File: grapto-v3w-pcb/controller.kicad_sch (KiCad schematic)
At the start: 31 parts, among them J5 Conn_01x06_Female, J6 USB_C_Receptacle_USB2.0, J7 USB_C_Receptacle_USB2.0, J8 Conn_01x06_Male, U11 USBLC6-4SC6, U12 ACN52840, U13 TPS2110, U14 LM3676SD-3.3

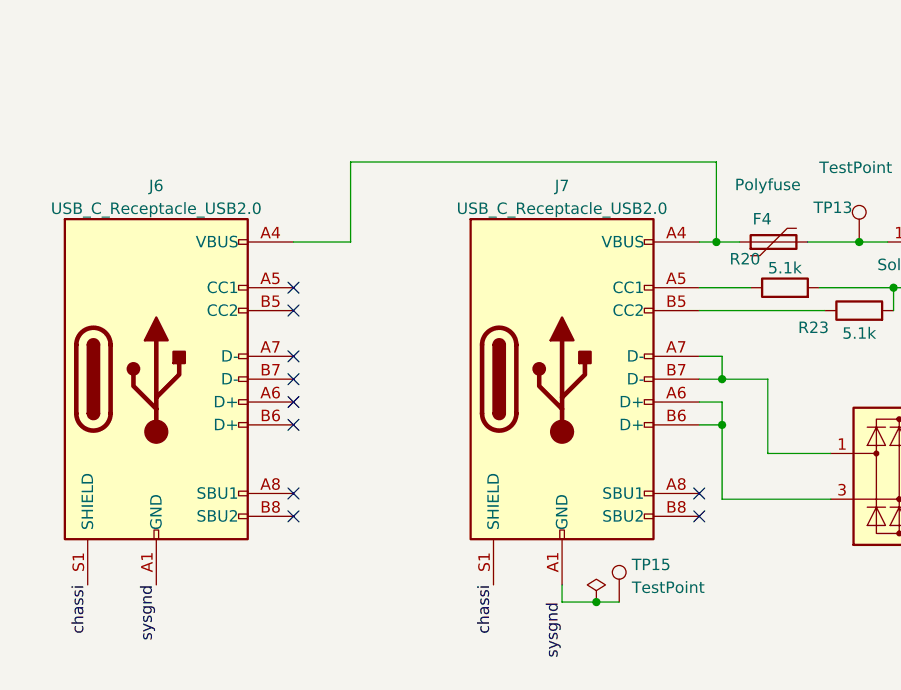
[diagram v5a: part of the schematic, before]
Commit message: Began case rework.
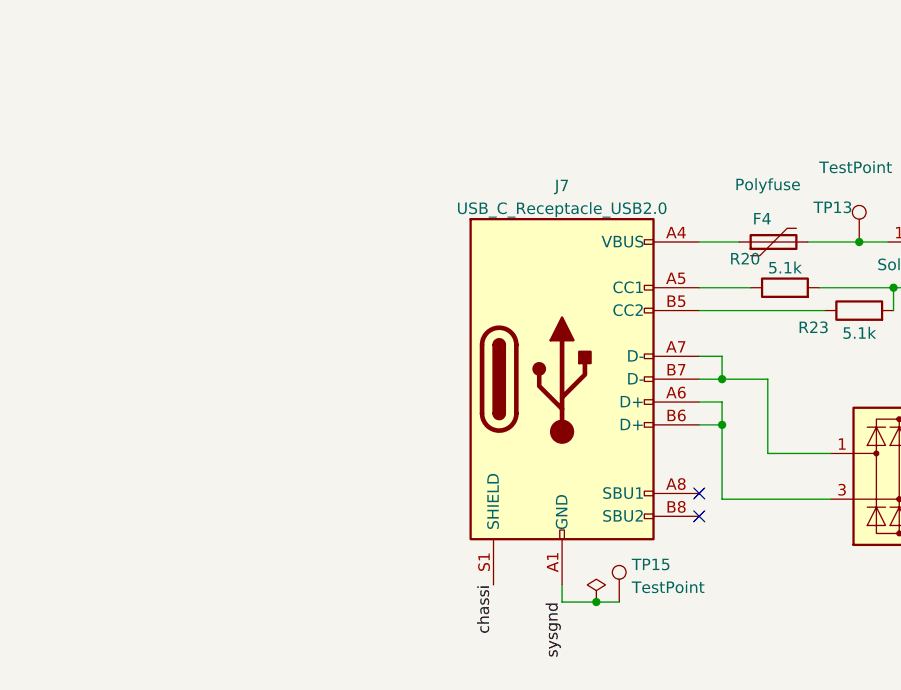
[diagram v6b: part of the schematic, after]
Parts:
- removed J6: USB_C_Receptacle_USB2.0, grapto-v3w:USB_C_Receptacle_molex_2169900001, symbol Connector:USB_C_Receptacle_USB2.0
- J7: footprint (none) -> grapto-v3w:USB_C_Receptacle_molex_2169900001
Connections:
- no-connect marks 23 -> 15
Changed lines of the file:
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@@
   (junction (at 100.965 157.48) (diameter 0) (color 0 0 0 0)
   )
-  (junction (at 100.33 137.16) (diameter 0) (color 0 0 0 0)
-  )
   (junction (at 149.86 59.69) (diameter 0) (color 0 0 0 0)
   )
-  (no_connect (at 53.34 149.86))
   (no_connect (at 38.1 45.72))
-  (no_connect (at 53.34 144.78))
   (no_connect (at 38.1 40.64))
-  (no_connect (at 53.34 154.94))
-  (no_connect (at 53.34 152.4))
-  (no_connect (at 53.34 167.64))
-  (no_connect (at 53.34 165.1))
   (no_connect (at 178.435 130.81))
   (no_connect (at 178.435 125.73))
@@
   (no_connect (at 201.295 143.51))
   (no_connect (at 203.835 143.51))
-  (no_connect (at 53.34 157.48))
   (no_connect (at 38.1 43.18))
   (no_connect (at 98.425 165.1))
   (no_connect (at 38.1 48.26))
-  (no_connect (at 53.34 142.24))
   (no_connect (at 98.425 167.64))
   (no_connect (at 124.46 36.195))
-  (wire (pts (xy 100.33 128.27) (xy 100.33 137.16))
-    (stroke (width 0) (type default) (color 0 0 0 0))
-  )
   (wire (pts (xy 98.425 154.94) (xy 100.965 154.94))
     (stroke (width 0) (type default) (color 0 0 0 0))
@@
     (stroke (width 0) (type default) (color 0 0 0 0))
   )
-  (wire (pts (xy 100.33 137.16) (xy 102.87 137.16))
-    (stroke (width 0) (type default) (color 0 0 0 0))
-  )
   (wire (pts (xy 243.205 54.61) (xy 243.205 58.42))
     (stroke (width 0) (type default) (color 0 0 0 0))
@@
     (stroke (width 0) (type default) (color 0 0 0 0))
   )
-  (wire (pts (xy 59.69 137.16) (xy 59.69 128.27))
-    (stroke (width 0) (type default) (color 0 0 0 0))
-  )
   (wire (pts (xy 45.72 55.245) (xy 45.72 49.53))
     (stroke (width 0) (type default) (color 0 0 0 0))
@@
     (stroke (width 0) (type default) (color 0 0 0 0))
   )
-  (wire (pts (xy 59.69 128.27) (xy 100.33 128.27))
-    (stroke (width 0) (type default) (color 0 0 0 0))
-  )
   (wire (pts (xy 165.735 43.815) (xy 165.735 45.085))
     (stroke (width 0) (type default) (color 0 0 0 0))
@@
     (stroke (width 0) (type default) (color 0 0 0 0))
   )
-  (wire (pts (xy 53.34 137.16) (xy 59.69 137.16))
-    (stroke (width 0) (type default) (color 0 0 0 0))
-  )
   (wire (pts (xy 114.935 59.69) (xy 114.935 59.055))
     (stroke (width 0) (type default) (color 0 0 0 0))
@@
     (stroke (width 0) (type default) (color 0 0 0 0))
   )
-  (wire (pts (xy 98.425 137.16) (xy 100.33 137.16))
+  (wire (pts (xy 98.425 137.16) (xy 102.87 137.16))
     (stroke (width 0) (type default) (color 0 0 0 0))
   )
@@
     (effects (font (size 1.27 1.27)) (justify right bottom))
   )
-  (label "sysgnd" (at 38.1 175.26 270)
-    (effects (font (size 1.27 1.27)) (justify right bottom))
-  )
   (label "col0" (at 178.435 107.95 180)
     (effects (font (size 1.27 1.27)) (justify right bottom))
@@
     (effects (font (size 1.27 1.27)) (justify right bottom))
   )
-  (label "chassi" (at 30.48 175.26 270)
-    (effects (font (size 1.27 1.27)) (justify right bottom))
-  )
   (label "3.3v" (at 178.435 133.35 180)
     (effects (font (size 1.27 1.27)) (justify right bottom))
@@
   (label "p+" (at 165.735 52.07 0)
     (effects (font (size 1.27 1.27)) (justify left bottom))
-  )
-  (symbol (lib_id "Connector:USB_C_Receptacle_USB2.0") (at 38.1 152.4 0) (unit 1)
-    (in_bom yes) (on_board yes) (fields_autoplaced)
-    (property "Reference" "J6" (id 0) (at 38.1 130.9202 0))
-    (property "Value" "USB_C_Receptacle_USB2.0" (id 1) (at 38.1 133.4571 0))
-    (property "Footprint" "grapto-v3w:USB_C_Receptacle_molex_2169900001" (id 2) (at 41.91 152.4 0)
-      (effects (font (size 1.27 1.27)) hide)
-    )
-    (property "Datasheet" "https://www.usb.org/sites/default/files/documents/usb_type-c.zip" (id 3) (at 41.91 152.4 0)
-      (effects (font (size 1.27 1.27)) hide)
-    )
-    (pin "A1")
-    (pin "A12")
-    (pin "A4")
-    (pin "A5")
-    (pin "A6")
-    (pin "A7")
-    (pin "A8")
-    (pin "A9")
-    (pin "B1")
-    (pin "B12")
-    (pin "B4")
-    (pin "B5")
-    (pin "B6")
-    (pin "B7")
-    (pin "B8")
-    (pin "B9")
-    (pin "S1")
   )
   (symbol (lib_id "Device:R") (at 106.68 50.8 0) (unit 1)
@@
     (property "Reference" "J7" (id 0) (at 83.185 130.9202 0))
     (property "Value" "USB_C_Receptacle_USB2.0" (id 1) (at 83.185 133.4571 0))
-    (property "Footprint" "" (id 2) (at 86.995 152.4 0)
-      (effects (font (size 1.27 1.27)) hide)
-    )
+    (property "Footprint" "grapto-v3w:USB_C_Receptacle_molex_2169900001" (id 2) (at 86.995 152.4 0)
+      (effects (font (size 1.27 1.27)) hide)
+    )

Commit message: flipping usbs
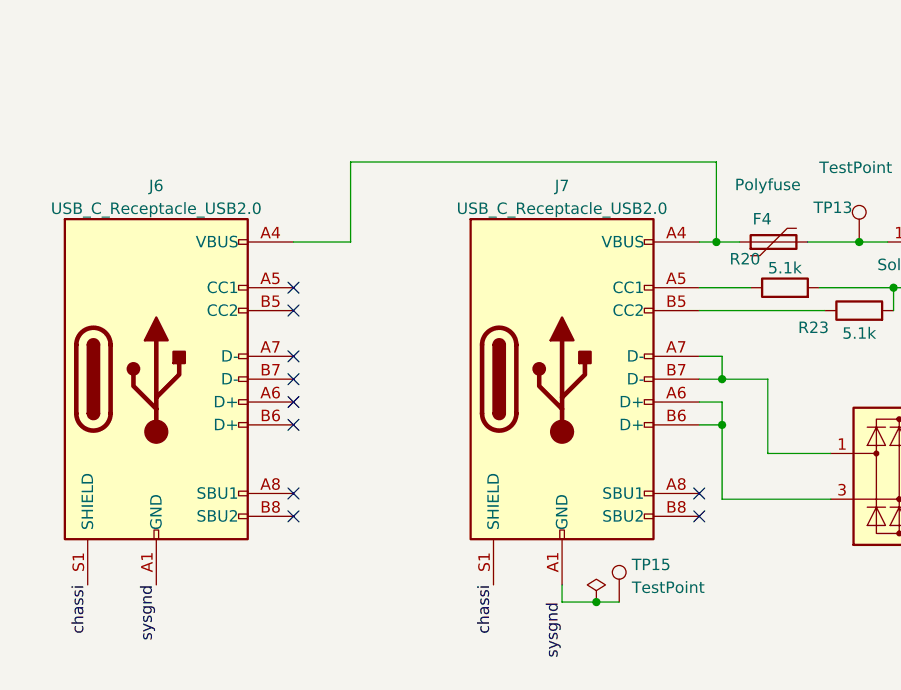
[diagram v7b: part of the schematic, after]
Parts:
- added J6: USB_C_Receptacle_USB2.0, grapto-v3w:USB_C_Receptacle_molex_2169900001, symbol Connector:USB_C_Receptacle_USB2.0
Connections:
- net chassi: now also J6.S1 (SHIELD)
- net sysgnd: now also J6.A1 (GND), J6.A12 (GND), J6.B1 (GND), J6.B12 (GND)
- net at F4.1, J7.A4 (VBUS), J7.A9 (VBUS)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: now also J6.A4 (VBUS), J6.A9 (VBUS), J6.B4 (VBUS), J6.B9 (VBUS)
- no-connect marks 15 -> 23
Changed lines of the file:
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@@
   (junction (at 100.965 157.48) (diameter 0) (color 0 0 0 0)
   )
+  (junction (at 100.33 137.16) (diameter 0) (color 0 0 0 0)
+  )
   (junction (at 149.86 59.69) (diameter 0) (color 0 0 0 0)
   )
+  (no_connect (at 53.34 149.86))
   (no_connect (at 38.1 45.72))
+  (no_connect (at 53.34 144.78))
   (no_connect (at 38.1 40.64))
+  (no_connect (at 53.34 154.94))
+  (no_connect (at 53.34 152.4))
+  (no_connect (at 53.34 167.64))
+  (no_connect (at 53.34 165.1))
   (no_connect (at 178.435 130.81))
   (no_connect (at 178.435 125.73))
@@
   (no_connect (at 201.295 143.51))
   (no_connect (at 203.835 143.51))
+  (no_connect (at 53.34 157.48))
   (no_connect (at 38.1 43.18))
   (no_connect (at 98.425 165.1))
   (no_connect (at 38.1 48.26))
+  (no_connect (at 53.34 142.24))
   (no_connect (at 98.425 167.64))
   (no_connect (at 124.46 36.195))
+  (wire (pts (xy 100.33 128.27) (xy 100.33 137.16))
+    (stroke (width 0) (type default) (color 0 0 0 0))
+  )
   (wire (pts (xy 98.425 154.94) (xy 100.965 154.94))
     (stroke (width 0) (type default) (color 0 0 0 0))
@@
     (stroke (width 0) (type default) (color 0 0 0 0))
   )
+  (wire (pts (xy 100.33 137.16) (xy 102.87 137.16))
+    (stroke (width 0) (type default) (color 0 0 0 0))
+  )
   (wire (pts (xy 243.205 54.61) (xy 243.205 58.42))
     (stroke (width 0) (type default) (color 0 0 0 0))
@@
     (stroke (width 0) (type default) (color 0 0 0 0))
   )
+  (wire (pts (xy 59.69 137.16) (xy 59.69 128.27))
+    (stroke (width 0) (type default) (color 0 0 0 0))
+  )
   (wire (pts (xy 45.72 55.245) (xy 45.72 49.53))
     (stroke (width 0) (type default) (color 0 0 0 0))
@@
     (stroke (width 0) (type default) (color 0 0 0 0))
   )
+  (wire (pts (xy 59.69 128.27) (xy 100.33 128.27))
+    (stroke (width 0) (type default) (color 0 0 0 0))
+  )
   (wire (pts (xy 165.735 43.815) (xy 165.735 45.085))
     (stroke (width 0) (type default) (color 0 0 0 0))
@@
     (stroke (width 0) (type default) (color 0 0 0 0))
   )
+  (wire (pts (xy 53.34 137.16) (xy 59.69 137.16))
+    (stroke (width 0) (type default) (color 0 0 0 0))
+  )
   (wire (pts (xy 114.935 59.69) (xy 114.935 59.055))
     (stroke (width 0) (type default) (color 0 0 0 0))
@@
     (stroke (width 0) (type default) (color 0 0 0 0))
   )
-  (wire (pts (xy 98.425 137.16) (xy 102.87 137.16))
+  (wire (pts (xy 98.425 137.16) (xy 100.33 137.16))
     (stroke (width 0) (type default) (color 0 0 0 0))
   )
@@
     (effects (font (size 1.27 1.27)) (justify right bottom))
   )
+  (label "sysgnd" (at 38.1 175.26 270)
+    (effects (font (size 1.27 1.27)) (justify right bottom))
+  )
   (label "col0" (at 178.435 107.95 180)
     (effects (font (size 1.27 1.27)) (justify right bottom))
@@
     (effects (font (size 1.27 1.27)) (justify right bottom))
   )
+  (label "chassi" (at 30.48 175.26 270)
+    (effects (font (size 1.27 1.27)) (justify right bottom))
+  )
   (label "3.3v" (at 178.435 133.35 180)
     (effects (font (size 1.27 1.27)) (justify right bottom))
@@
     (effects (font (size 1.27 1.27)) (justify left bottom))
   )
+  (symbol (lib_id "Connector:USB_C_Receptacle_USB2.0") (at 38.1 152.4 0) (unit 1)
+    (in_bom yes) (on_board yes) (fields_autoplaced)
+    (property "Reference" "J6" (id 0) (at 38.1 130.9202 0))
+    (property "Value" "USB_C_Receptacle_USB2.0" (id 1) (at 38.1 133.4571 0))
+    (property "Footprint" "grapto-v3w:USB_C_Receptacle_molex_2169900001" (id 2) (at 41.91 152.4 0)
+      (effects (font (size 1.27 1.27)) hide)
+    )
+    (property "Datasheet" "https://www.usb.org/sites/default/files/documents/usb_type-c.zip" (id 3) (at 41.91 152.4 0)
+      (effects (font (size 1.27 1.27)) hide)
+    )
+    (pin "A1")
+    (pin "A12")
+    (pin "A4")
+    (pin "A5")
+    (pin "A6")
+    (pin "A7")
+    (pin "A8")
+    (pin "A9")
+    (pin "B1")
+    (pin "B12")
+    (pin "B4")
+    (pin "B5")
+    (pin "B6")
+    (pin "B7")
+    (pin "B8")
+    (pin "B9")
+    (pin "S1")
+  )
   (symbol (lib_id "Device:R") (at 106.68 50.8 0) (unit 1)

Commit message: Added snap supports.
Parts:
- added TP19: ~, symbol Connector:TestPoint
- added TP20, TP21: (no value), symbol Connector:TestPoint
- TP13, TP14, TP15, TP16, TP17, TP18: footprint TestPoint:TestPoint_Pad_2.0x2.0mm -> (none)
- U12: footprint grapto-v3w:ACN52840_mirror -> (none)
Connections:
- net low_batt: now also TP19.1
- net scl: now also TP20.1
- net sda: now also TP21.1
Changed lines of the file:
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@@
+    (stroke (width 0) (type default) (color 0 0 0 0))
+  )
+  (wire (pts (xy 72.39 38.1) (xy 83.82 38.1))
     (stroke (width 0) (type default) (color 0 0 0 0))
   )
@@
     (effects (font (size 1.27 1.27)) (justify right bottom))
   )
-  (label "scl" (at 250.825 120.65 180)
+  (label "scl" (at 250.825 118.745 180)
     (effects (font (size 1.27 1.27)) (justify right bottom))
   )
@@
     (effects (font (size 1.27 1.27)) (justify left bottom))
   )
-  (label "sda" (at 258.445 120.65 0)
+  (label "sda" (at 258.445 118.745 0)
     (effects (font (size 1.27 1.27)) (justify left bottom))
   )
@@
       (effects (font (size 1.27 1.27)) (justify left))
     )
-    (property "Footprint" "TestPoint:TestPoint_Pad_2.0x2.0mm" (id 2) (at 255.905 46.99 0)
+    (property "Footprint" "" (id 2) (at 255.905 46.99 0)
       (effects (font (size 1.27 1.27)) hide)
     )
@@
     (pin "2")
   )
+  (symbol (lib_id "Connector:TestPoint") (at 258.445 120.65 270) (unit 1)
+    (in_bom yes) (on_board yes) (fields_autoplaced)
+    (property "Reference" "TP21" (id 0) (at 263.144 119.8153 90)
+      (effects (font (size 1.27 1.27)) (justify left))
+    )
+    (property "Value" "" (id 1) (at 263.144 122.3522 90)
+      (effects (font (size 1.27 1.27)) (justify left))
+    )
+    (property "Footprint" "" (id 2) (at 258.445 125.73 0)
+      (effects (font (size 1.27 1.27)) hide)
+    )
+    (property "Datasheet" "~" (id 3) (at 258.445 125.73 0)
+      (effects (font (size 1.27 1.27)) hide)
+    )
+    (pin "1")
+  )
   (symbol (lib_id "Device:C") (at 243.205 50.8 0) (unit 1)
     (in_bom yes) (on_board yes) (fields_autoplaced)
@@
     (pin "1")
     (pin "2")
+  )
+  (symbol (lib_id "Connector:TestPoint") (at 83.82 38.1 0) (unit 1)
+    (in_bom yes) (on_board yes)
+    (property "Reference" "TP19" (id 0) (at 84.455 31.75 90))
+    (property "Value" "~" (id 1) (at 81.915 34.925 90))
+    (property "Footprint" "" (id 2) (at 88.9 38.1 0)
+      (effects (font (size 1.27 1.27)) hide)
+    )
+    (property "Datasheet" "~" (id 3) (at 88.9 38.1 0)
+      (effects (font (size 1.27 1.27)) hide)
+    )
+    (pin "1")
   )
   (symbol (lib_id "Connector:USB_C_Receptacle_USB2.0") (at 83.185 152.4 0) (unit 1)
@@
     (property "Reference" "U12" (id 0) (at 198.12 99.221 0))
     (property "Value" "ACN52840" (id 1) (at 198.12 101.7579 0))
-    (property "Footprint" "grapto-v3w:ACN52840_mirror" (id 2) (at 207.645 147.32 0)
+    (property "Footprint" "" (id 2) (at 207.645 147.32 0)
       (effects (font (size 1.27 1.27)) hide)
     )
@@
       (effects (font (size 1.27 1.27)) (justify left))
     )
-    (property "Footprint" "TestPoint:TestPoint_Pad_2.0x2.0mm" (id 2) (at 94.615 177.165 0)
+    (property "Footprint" "" (id 2) (at 94.615 177.165 0)
       (effects (font (size 1.27 1.27)) hide)
     )
@@
       (effects (font (size 1.27 1.27)) (justify left))
     )
-    (property "Footprint" "TestPoint:TestPoint_Pad_2.0x2.0mm" (id 2) (at 135.255 137.16 0)
+    (property "Footprint" "" (id 2) (at 135.255 137.16 0)
       (effects (font (size 1.27 1.27)) hide)
     )
@@
       (effects (font (size 1.27 1.27)) (justify left))
     )
-    (property "Footprint" "TestPoint:TestPoint_Pad_2.0x2.0mm" (id 2) (at 121.285 137.16 0)
+    (property "Footprint" "" (id 2) (at 121.285 137.16 0)
       (effects (font (size 1.27 1.27)) hide)
     )
     (property "Datasheet" "~" (id 3) (at 121.285 137.16 0)
+      (effects (font (size 1.27 1.27)) hide)
+    )
+    (pin "1")
+  )
+  (symbol (lib_id "Connector:TestPoint") (at 250.825 120.65 90) (unit 1)
+    (in_bom yes) (on_board yes)
+    (property "Reference" "TP20" (id 0) (at 244.475 120.015 90))
+    (property "Value" "" (id 1) (at 247.65 122.555 90))
+    (property "Footprint" "" (id 2) (at 250.825 115.57 0)
+      (effects (font (size 1.27 1.27)) hide)
+    )
+    (property "Datasheet" "~" (id 3) (at 250.825 115.57 0)
       (effects (font (size 1.27 1.27)) hide)
     )
@@
       (effects (font (size 1.27 1.27)) (justify left))
     )
-    (property "Footprint" "TestPoint:TestPoint_Pad_2.0x2.0mm" (id 2) (at 200.025 46.99 0)
+    (property "Footprint" "" (id 2) (at 200.025 46.99 0)
       (effects (font (size 1.27 1.27)) hide)
     )
@@
       (effects (font (size 1.27 1.27)) (justify left))
     )
-    (property "Footprint" "TestPoint:TestPoint_Pad_2.0x2.0mm" (id 2) (at 269.875 46.99 0)
-      (effects (font (size 1.27 1.27)) hide)
-    )
+    (property "Footprint" "" (id 2) (at 269.875 46.99 0)
+      (effects (font (size 1.27 1.27)) hide)
+    )
